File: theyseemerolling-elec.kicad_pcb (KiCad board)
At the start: 2 copper layers, 80 x 50 mm, 75 parts, among them IC2 L6205PD, J2 Conn_01x02, J3 Conn_01x08, J4 Conn_01x02, J5 Conn_01x02, P1 CAN_conn, P2 CAN_conn, Q1 BSS138, U1 STM32F303K8Tx, U2 LD1117S50TR_SOT223, U3 ACS711xLCTR-12AB, U4 ACS711xLCTR-12AB, U5 74HC00, U6 LD1117S33TR_SOT223, U7 MCP2551-I-SN, U8 AT25SF041

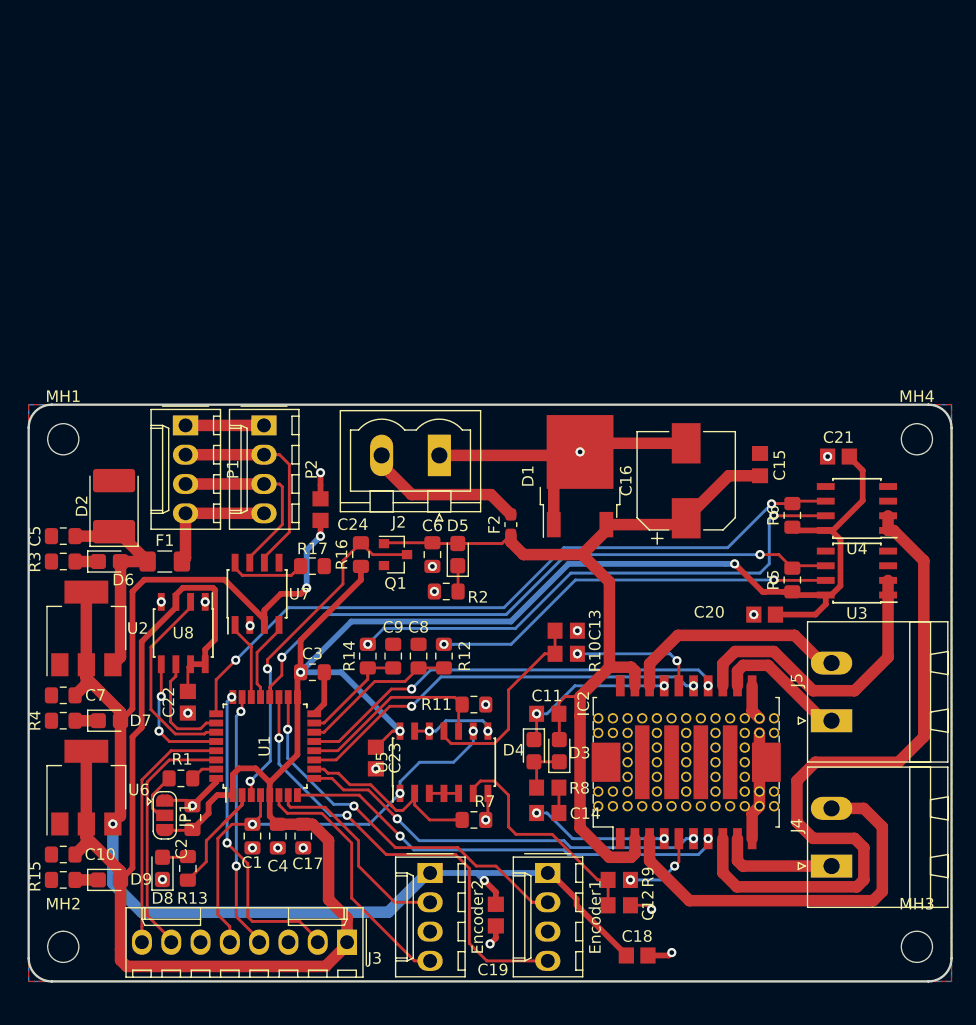
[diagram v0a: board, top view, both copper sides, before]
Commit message: cleanup pcb, reorganize text
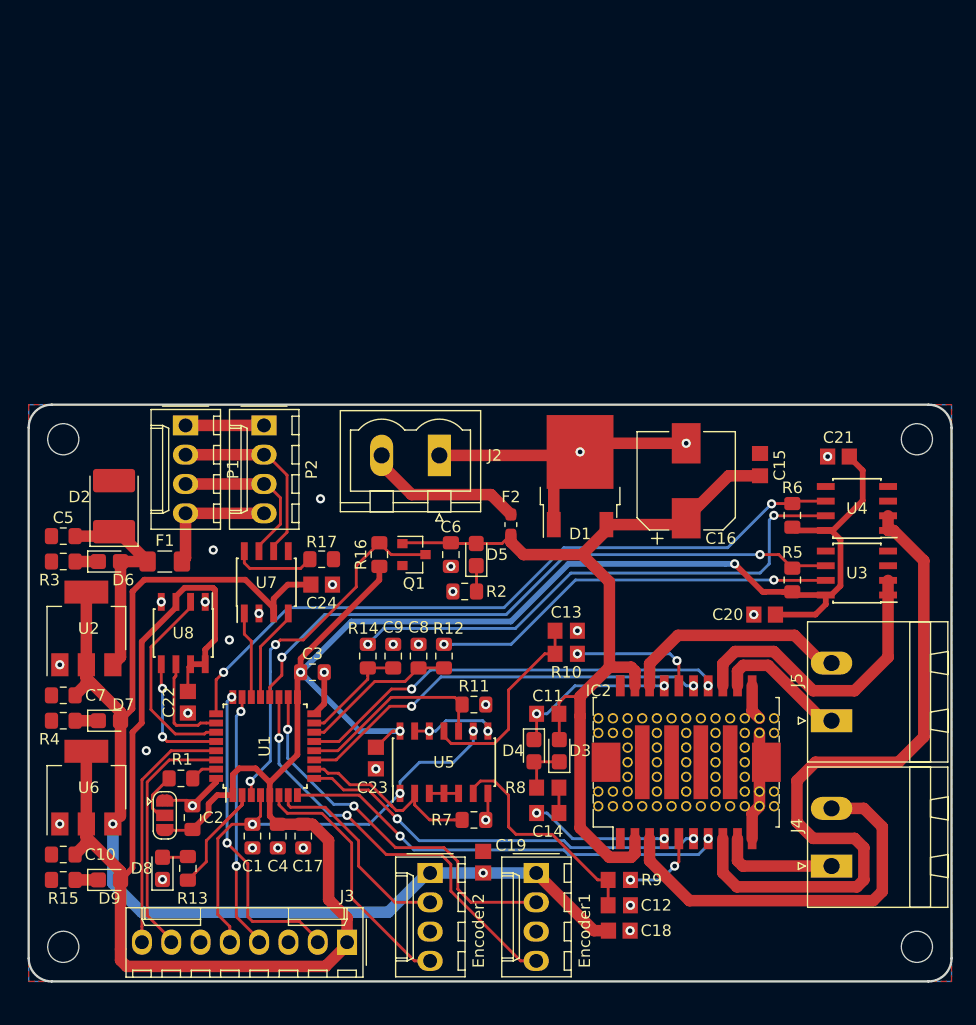
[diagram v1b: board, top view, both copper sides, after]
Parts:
- moved C24 6.50 mm to (125.4, 65.6), turned to 0 degrees
- moved C19 4.72 mm to (139.4, 89.7), turned to 90 degrees
- moved C18 2.65 mm to (151.2, 95.6)
- moved D5 1.60 mm to (138.8, 63.0)
- moved R2 1.60 mm to (137.8, 66.2)
- moved C6 1.60 mm to (136.6, 63.0)
- moved Q1 1.60 mm to (133.4, 63.0)
- moved R16 1.60 mm to (130.4, 63.0)
- moved U7 1.28 mm to (120.6, 65.4)
- moved R17 1.00 mm to (125.4, 63.4)
- moved Encoder1 1.00 mm to (144.0, 90.6)
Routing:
- net +5V: track 120.1 -> 107.1 mm, vias 4 -> 2
- net GND: track 69.2 -> 61.0 mm, vias 22 -> 31
- net /f3/Encoder_1_B: track 40.0 -> 36.5 mm
- net Net-(P1-Pad2): track 18.8 -> 16.6 mm
- net Net-(P1-Pad3): track 16.2 -> 14.1 mm
- net /f3/Encoder_1_A: track 33.0 -> 34.8 mm
- net /f3/ABOUT_DA_POWER: track 30.5 -> 32.2 mm
- net VCC: track 79.0 -> 77.4 mm
- net /f3/CAN_RX: track 7.16 -> 8.26 mm
- net /f3/CAN_TX: track 6.83 -> 7.50 mm
- net /f3/SCK: track 9.60 -> 8.98 mm
- net +3V3: track 226.3 -> 226.9 mm

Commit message: Add text and logos
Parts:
- added LOGO1: Logo_Open_Hardware_Large, Symbol:OSHW-Logo_7.5x8mm_SilkScreen, B.Cu at (146.6, 58.4)
- added LOGO2: Logo_Open_Hardware_Small, PhoenixRobotik:Logo_14,5mm, B.Cu at (158.6, 60.1)
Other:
- board text added: "Phenix Robotik"
- board text added: "TheySeeMeRolling"
- board text added: "https://github.com/PhenixRobotik/theyseemerolling-elec"

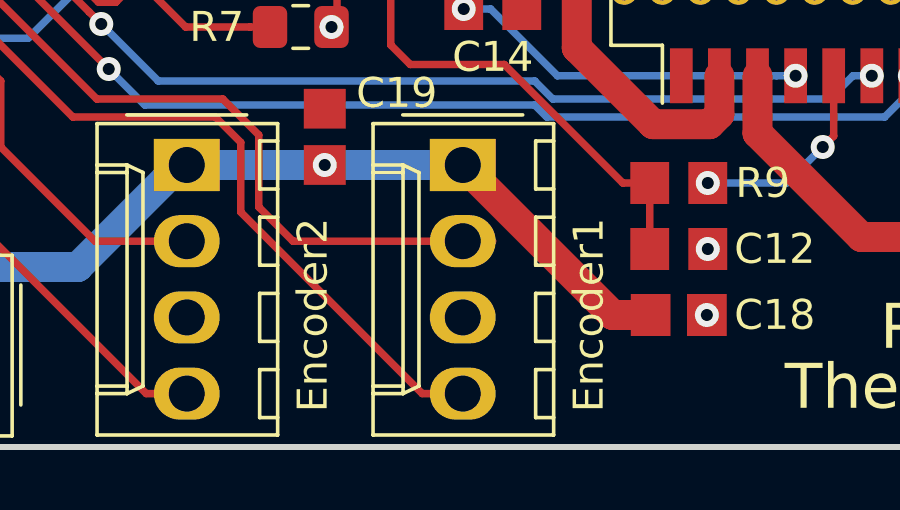
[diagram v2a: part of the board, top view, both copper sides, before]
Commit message: rename components
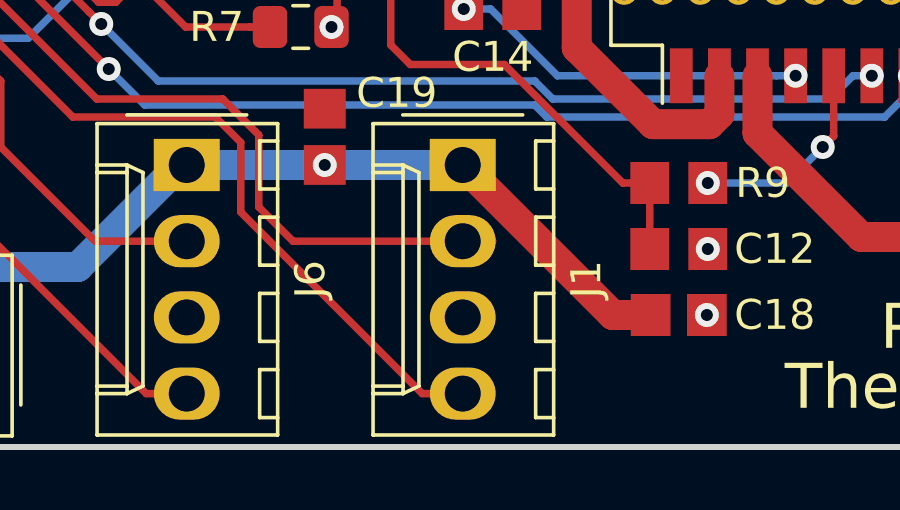
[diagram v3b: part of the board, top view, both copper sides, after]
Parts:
- removed Encoder1, Encoder2: Conn_01x04, Connector_Molex:Molex_KK-254_AE-6410-04A_1x04_P2.54mm_Vertical
- added J1: Conn_Encoder1, Connector_Molex:Molex_KK-254_AE-6410-04A_1x04_P2.54mm_Vertical, F.Cu at (144.0, 90.6)
- added J6: Conn_Encoder2, Connector_Molex:Molex_KK-254_AE-6410-04A_1x04_P2.54mm_Vertical, F.Cu at (134.8, 90.6)
- J2: value Conn_01x02 -> Conn_Power_In
- J3: value Conn_01x08 -> Conn_SWD_UART
- J4: value Conn_01x02 -> Conn_Mot1
- J5: value Conn_01x02 -> Conn_Mot2
- JP1: value Jumper_NC_Dual -> JP_Select_Boot
- R12, R14: value R -> R_Sense
- R15, R2, R3, R4: value R -> R_LED

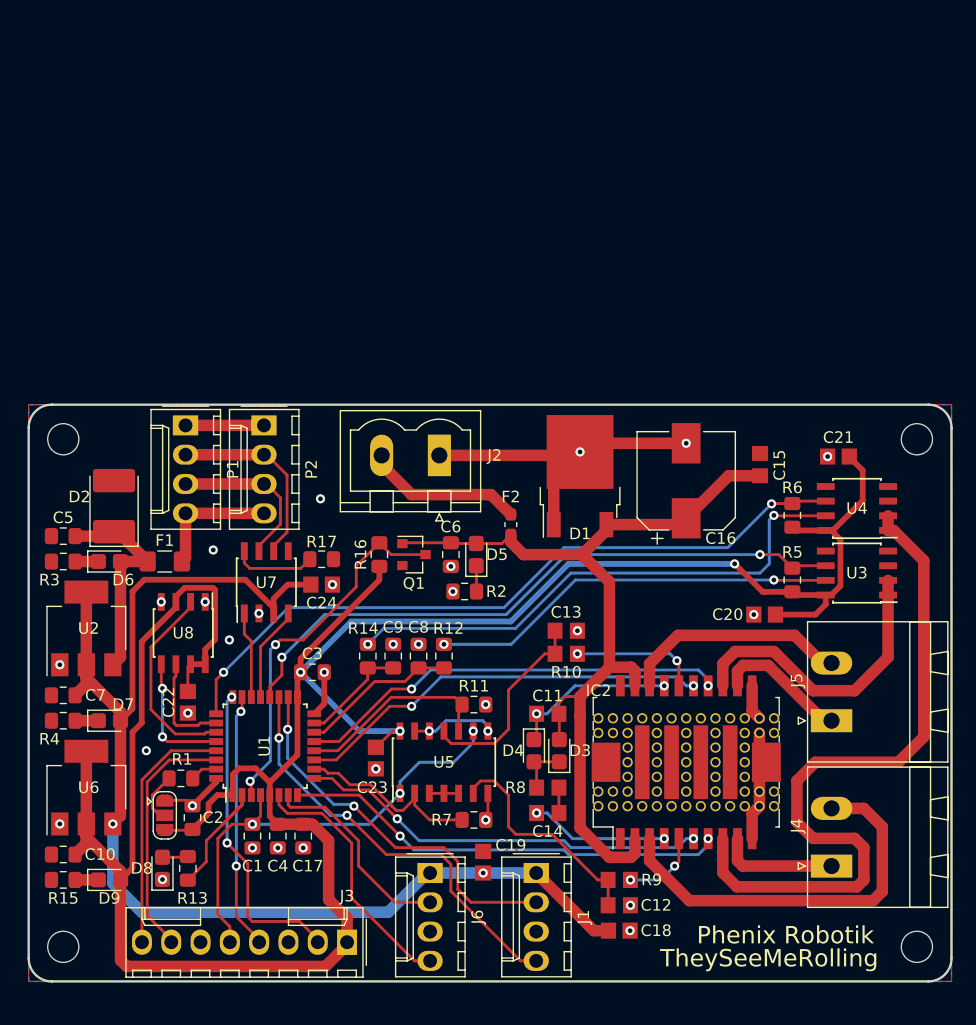
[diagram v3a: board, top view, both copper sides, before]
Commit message: Use JST_PH connectors for encoders. Re-route with new connectors.
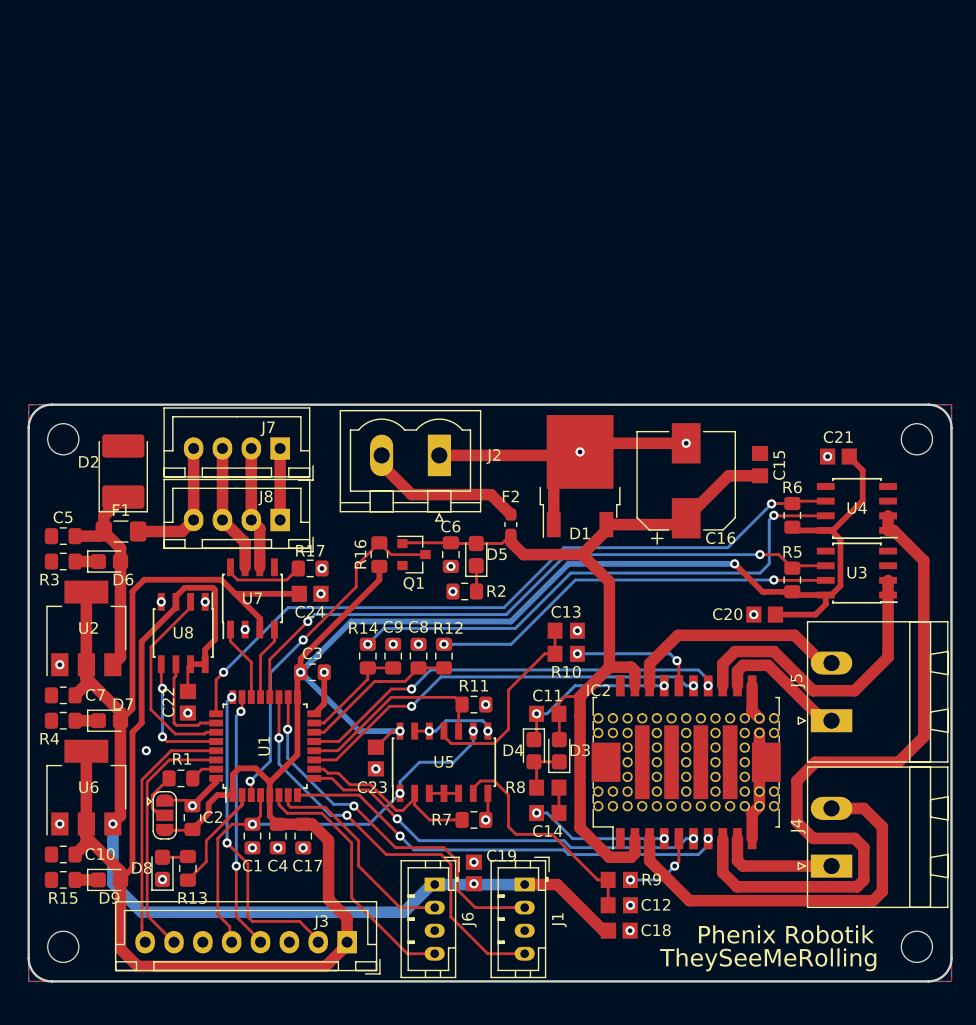
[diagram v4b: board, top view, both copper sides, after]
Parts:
- removed P1, P2: CAN_conn, Connector_Molex:Molex_KK-254_AE-6410-04A_1x04_P2.54mm_Vertical
- added J7: CAN_conn, Connector_JST:JST_XH_B04B-XH-A_1x04_P2.50mm_Vertical, F.Cu at (121.8, 53.8)
- added J8: CAN_conn, Connector_JST:JST_XH_B04B-XH-A_1x04_P2.50mm_Vertical, F.Cu at (121.8, 60.0)
- J1, J6: footprint Connector_Molex:Molex_KK-254_AE-6410-04A_1x04_P2.54mm_Vertical -> Connector_JST:JST_PH_B4B-PH-K_1x04_P2.00mm_Vertical
- J3: footprint Connector_Molex:Molex_KK-254_AE-6410-08A_1x08_P2.54mm_Vertical -> Connector_JST:JST_XH_B08B-XH-A_1x08_P2.50mm_Vertical
- moved F1 4.60 mm to (108.0, 61.0)
- moved D2 3.10 mm to (108.2, 55.8)
- moved U7 1.84 mm to (119.4, 66.8)
- moved J1 1.41 mm to (143.0, 91.6)
- moved C24 1.28 mm to (124.4, 66.4)
- moved R17 1.28 mm to (124.4, 64.2)
- moved C19 1.23 mm to (138.6, 90.6)
- moved J6 1.08 mm to (135.2, 91.6)
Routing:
- net Net-(J7-Pad2): track 16.6 -> 10.8 mm
- net Net-(J7-Pad3): track 14.1 -> 11.3 mm
- net /f3/Encoder_1_A: track 34.8 -> 32.7 mm
- net /f3/CAN_RX: track 8.26 -> 6.35 mm
- net /f3/ABOUT_DA_POWER: track 32.2 -> 31.0 mm
- net /f3/CAN_TX: track 7.50 -> 6.60 mm
- net +5V: track 107.1 -> 106.5 mm
- net /f3/Encoder_2_A: track 17.9 -> 18.5 mm
- net +3V3: track 226.9 -> 226.3 mm
- net GND: track 61.0 -> 60.6 mm, vias 31 -> 30

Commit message: level conversion, to check and route
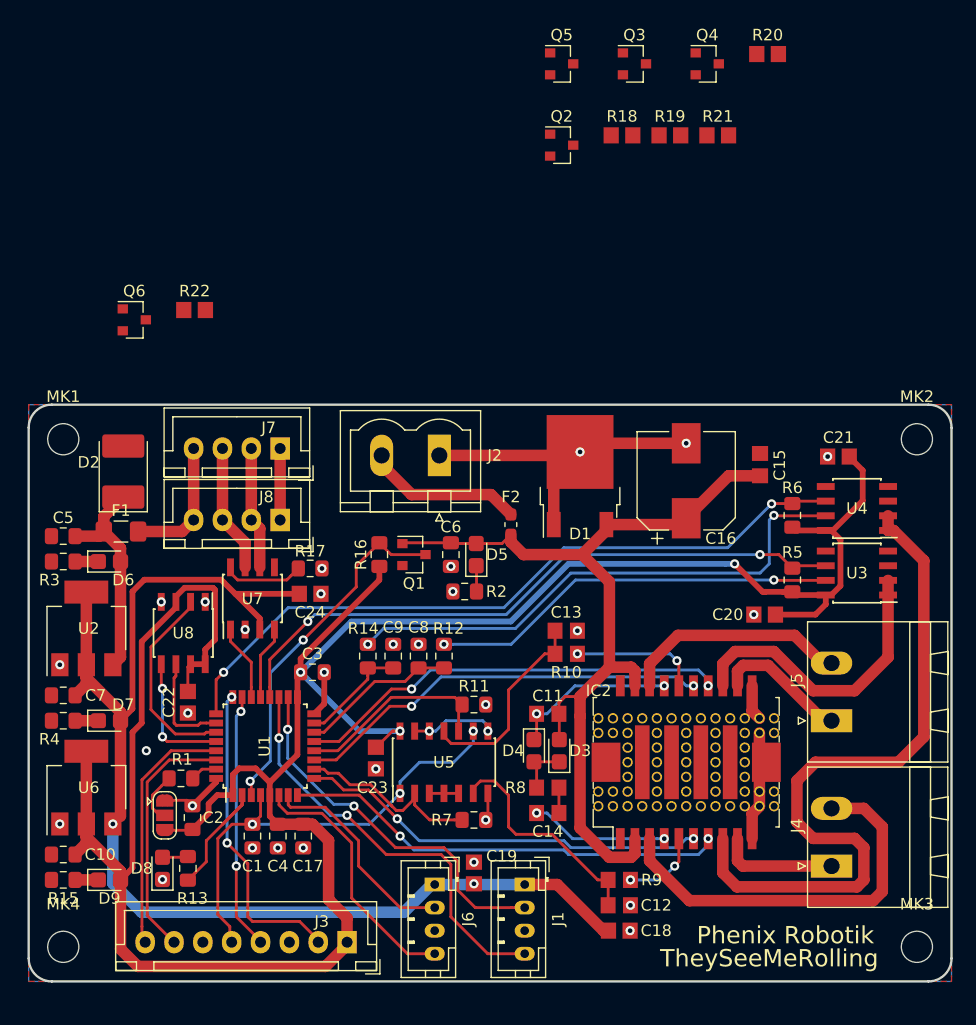
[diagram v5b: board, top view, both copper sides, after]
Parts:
- removed MH1, MH2, MH3, MH4: MountingHole, MountingHole:MountingHole_2.7mm_M2.5
- added MK1: Mounting_Hole, MountingHole:MountingHole_2.7mm_M2.5, F.Cu at (103.0, 53.0)
- added MK2: Mounting_Hole, MountingHole:MountingHole_2.7mm_M2.5, F.Cu at (177.0, 53.0)
- added MK3: Mounting_Hole, MountingHole:MountingHole_2.7mm_M2.5, F.Cu at (177.0, 97.0)
- added MK4: Mounting_Hole, MountingHole:MountingHole_2.7mm_M2.5, F.Cu at (103.0, 97.0)
- added Q2: BSS138, Package_TO_SOT_SMD:SOT-23, F.Cu at (146.2, 27.5)
- added Q3: BSS138, Package_TO_SOT_SMD:SOT-23, F.Cu at (152.5, 20.5)
- added Q4: BSS138, Package_TO_SOT_SMD:SOT-23, F.Cu at (158.8, 20.5)
- added Q5: BSS138, Package_TO_SOT_SMD:SOT-23, F.Cu at (146.2, 20.5)
- added Q6: BSS138, Package_TO_SOT_SMD:SOT-23, F.Cu at (109.2, 42.6)
- added R18: R, Resistor_SMD:R_0805_2012Metric_Pad1.33x1.40mm_HandSolder, F.Cu at (151.4, 26.7)
- added R19: R, Resistor_SMD:R_0805_2012Metric_Pad1.33x1.40mm_HandSolder, F.Cu at (155.6, 26.7)
- added R20: R, Resistor_SMD:R_0805_2012Metric_Pad1.33x1.40mm_HandSolder, F.Cu at (164.1, 19.6)
- added R21: R, Resistor_SMD:R_0805_2012Metric_Pad1.33x1.40mm_HandSolder, F.Cu at (159.7, 26.7)
- added R22: R, Resistor_SMD:R_0805_2012Metric_Pad1.33x1.40mm_HandSolder, F.Cu at (114.4, 41.8)
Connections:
- U1 pad 18: /f3/Encoder_1_A -> Net-(Q4-Pad2)
- U1 pad 19: /f3/Encoder_1_B -> Net-(Q5-Pad2)
- U1 pad 6: /f3/Encoder_2_B -> Net-(Q2-Pad2)
- U1 pad 7: /f3/Encoder_2_A -> Net-(Q3-Pad2)
- U7 pad 4: /f3/CAN_RX -> Net-(Q6-Pad3)

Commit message: correction, to route
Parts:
- added R23: R, Resistor_SMD:R_0805_2012Metric_Pad1.33x1.40mm_HandSolder, F.Cu at (104.0, 36.0)
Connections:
- R22 pad 1: Net-(Q6-Pad3) -> /f3/CAN_RX
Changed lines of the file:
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@@
     (tracks 598)
     (zones 0)
-    (modules 87)
+    (modules 88)
     (nets 69)
   )
@@
     (add_net VCC)
   )
+  (module Resistor_SMD:R_0805_2012Metric_Pad1.33x1.40mm_HandSolder (layer F.Cu)
+    (at 104 36)
+    (descr "Resistor SMD 0805 (2012 Metric), square (rectangular) end terminal, IPC_7351 nominal with elongated pad for handsoldering. (Body size source: http://www.tortai-tech.com/upload/download/2011102023233369053.pdf), generated with kicad-footprint-generator")
+    (tags "resistor handsolder")
+    (attr smd)
+    (fp_text reference R23 (at 0 -1.65) (layer F.SilkS)
+      (effects (font (size 1 1) (thickness 0.15)))
+    )
+    (fp_text value R (at 0 1.65) (layer F.Fab)
+      (effects (font (size 1 1) (thickness 0.15)))
+    )
+    (fp_line (start -1 0.6) (end -1 -0.6) (layer F.Fab) (width 0.1))
+    (fp_line (start -1 -0.6) (end 1 -0.6) (layer F.Fab) (width 0.1))
+    (fp_line (start 1 -0.6) (end 1 0.6) (layer F.Fab) (width 0.1))
+    (fp_line (start 1 0.6) (end -1 0.6) (layer F.Fab) (width 0.1))
+    (fp_line (start -1.85 0.95) (end -1.85 -0.95) (layer F.CrtYd) (width 0.05))
+    (fp_line (start -1.85 -0.95) (end 1.85 -0.95) (layer F.CrtYd) (width 0.05))
+    (fp_line (start 1.85 -0.95) (end 1.85 0.95) (layer F.CrtYd) (width 0.05))
+    (fp_line (start 1.85 0.95) (end -1.85 0.95) (layer F.CrtYd) (width 0.05))
+    (fp_text user %R (at 0 0) (layer F.Fab)
+      (effects (font (size 0.5 0.5) (thickness 0.08)))
+    )
+    (pad 1 smd rect (at -0.9375 0) (size 1.325 1.4) (layers F.Cu F.Paste F.Mask)
+      (net 64 "Net-(Q6-Pad3)"))
+    (pad 2 smd rect (at 0.9375 0) (size 1.325 1.4) (layers F.Cu F.Paste F.Mask)
+      (net 22 +5V))
+    (model ${KISYS3DMOD}/Resistor_SMD.3dshapes/R_0805_2012Metric.wrl
+      (at (xyz 0 0 0))
+      (scale (xyz 1 1 1))
+      (rotate (xyz 0 0 0))
+    )
+  )
   (module MountingHole:MountingHole_2.7mm_M2.5 (layer F.Cu)
     (at 177 53)
@@
     )
     (pad 1 smd rect (at -0.9375 0) (size 1.325 1.4) (layers F.Cu F.Paste F.Mask)
-      (net 64 "Net-(Q6-Pad3)"))
+      (net 49 /f3/CAN_RX))
     (pad 2 smd rect (at 0.9375 0) (size 1.325 1.4) (layers F.Cu F.Paste F.Mask)
       (net 19 +3V3))
